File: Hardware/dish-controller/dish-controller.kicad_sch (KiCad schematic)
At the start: 24 parts

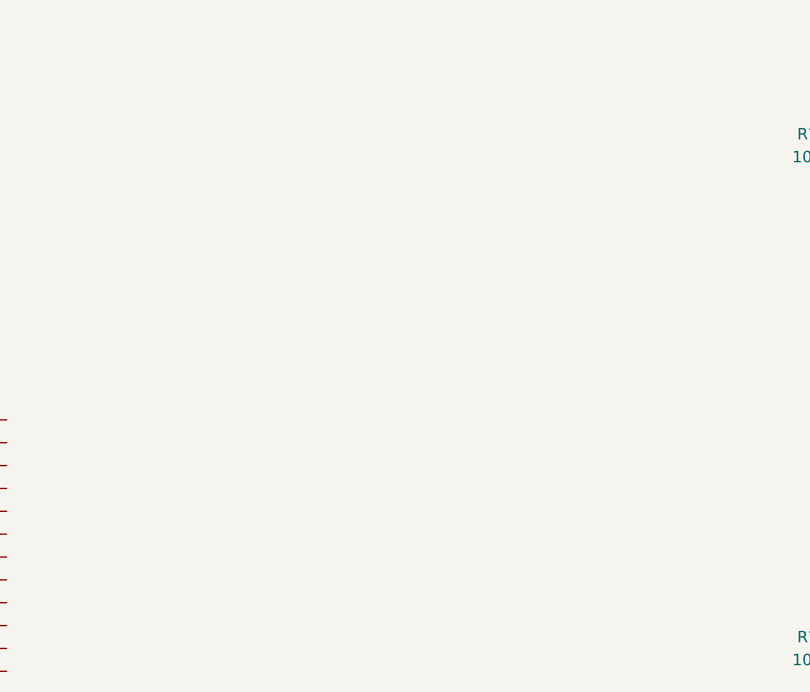
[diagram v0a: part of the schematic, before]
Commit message: Create encoder
COTS encoders are too expensive, so we are creating our own.
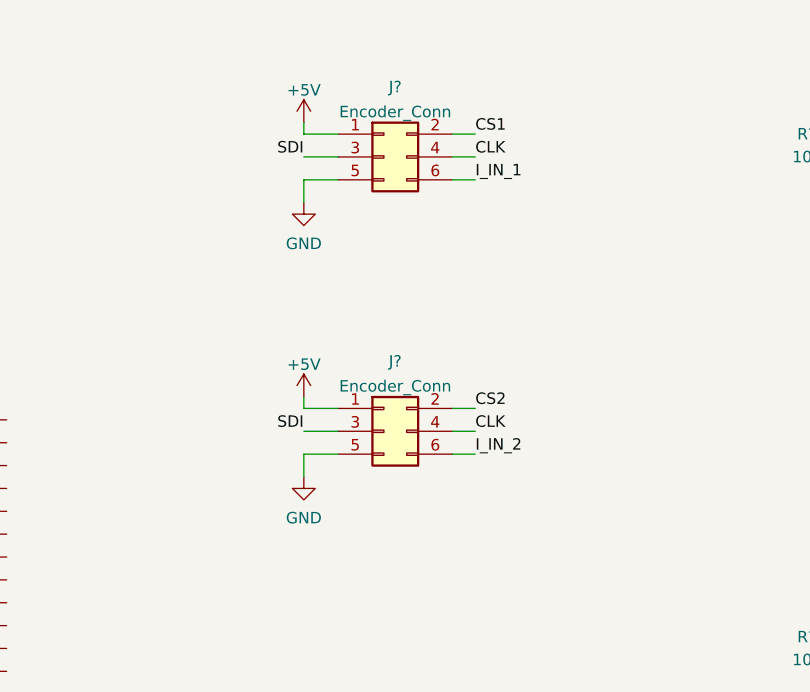
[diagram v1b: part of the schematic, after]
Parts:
- added J? (x2): Encoder_Conn, symbol Connector_Generic:Conn_02x03_Odd_Even
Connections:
- net +5V: now also J?.1 (Pin_1), J?.1 (Pin_1)
- net GND: now also J?.5 (Pin_5), J?.5 (Pin_5)
- new net CLK: J?.4 (Pin_4), J?.4 (Pin_4)
- new net CS1: J?.2 (Pin_2)
- new net CS2: J?.2 (Pin_2)
- new net I_IN_1: J?.6 (Pin_6)
- new net I_IN_2: J?.6 (Pin_6)
- new net SDI: J?.3 (Pin_3), J?.3 (Pin_3)

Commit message: Dish Controller ERC Pass
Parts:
- removed J? (x2): Encoder_Conn, symbol Connector_Generic:Conn_02x03_Odd_Even
- removed J?: Pi_GPIO, symbol Connector_Generic:Conn_02x20_Odd_Even
- removed R? (x8): 10k, symbol Device:R_Small
- added C1, C2, C3: 100u, symbol Device:C_Polarized_US
- added D1, D2, D3, D4: LED_Small, symbol Device:LED_Small
- added G1: DSES-Logo, interferometer:dses-logo, symbol interferometer:DSES-Logo
- added J3, J4: Encoder_Conn, symbol Connector_Generic:Conn_02x04_Odd_Even
- added R1: 3.3k, symbol Device:R_Small
- added R2: 10k, symbol Device:R_Small
- added R3, R4: 2k, symbol Device:R_Small
- added TP1, TP2, TP3, TP4, TP5, TP6, TP7, TP8, TP9: TestPoint, symbol Connector:TestPoint
- added U2: 74HCT541, symbol 74xx:74HCT541
- gave numbers to parts that had none: 15
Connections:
- net +12V: now also C1.1, C3.1, D2.2 (A)
- net +3V3: now also U1.1 (3V3)
- net +5V: now also U1.2 (5V), U1.4 (5V), C2.1, D1.2 (A), J3.1 (Pin_1), J4.1 (Pin_1), U2.20 (VCC)
- net A11: now also U1.33 (GPIO13)
- net A12: now also U1.37 (GPIO26)
- net A21: now also U1.35 (GPIO19)
- net A22: now also U1.40 (GPIO21)
- net CLK: now also U1.23 (GPIO11), TP5.1
- net GND: now also U1.14 (GND), U1.20 (GND), U1.25 (GND), U1.30 (GND), U1.34 (GND), U1.39 (GND), U1.6 (GND), U1.9 (GND), C1.2, C2.2, C3.2, J3.7 (Pin_7), J3.8 (Pin_8), J4.7 (Pin_7), J4.8 (Pin_8), R1.1, R2.2, R3.2, R4.1, U2.10 (GND)
- net IN11: now also U1.13 (GPIO27), TP1.1
- net IN12: now also U1.29 (GPIO5), TP6.1
- net IN21: now also U1.15 (GPIO22), TP2.1
- net IN22: now also U1.31 (GPIO6), TP7.1
- net PWM1: now also U1.3 (GPIO2)
- net PWM2: now also U1.5 (GPIO3)
- net SDI: now also U1.19 (GPIO10), TP3.1
- net STB1: now also U1.7 (GPIO4)
- net STB2: now also U1.11 (GPIO17)
- new net: D2.1 (K), R2.1
- new net: D3.1 (K), R3.1
- new net: D3.2 (A), U1.10 (GPIO15)
- new net: D1.1 (K), R1.2
- new net: D4.1 (K), R4.2
- new net: D4.2 (A), U1.12 (GPIO18)
- new net CLK_OUT: J3.4 (Pin_4), J4.4 (Pin_4), U2.17 (Y1)
- new net EPWM1_IN: J4.6 (Pin_6), U2.8 (A6)
- new net EPWM2_IN: J3.6 (Pin_6), U2.9 (A7)
- new net E_~{EN}: U1.38 (GPIO20), U2.1 (G1), U2.19 (G2)
- new net Logic Level Shift 1/HV1: U2.2 (A0)
- new net Logic Level Shift 1/HV2: U2.3 (A1)
- new net Logic Level Shift 1/HV3: U2.4 (A2)
- new net Logic Level Shift 1/HV4: U2.5 (A3)
- new net Logic Level Shift 2/HV1: U2.14 (Y4)
- new net Logic Level Shift 2/HV2: U2.13 (Y5)
- new net Logic Level Shift 2/HV3: U2.12 (Y6)
- new net Logic Level Shift 2/HV4: U2.11 (Y7)
- new net SDI_OUT: J3.2 (Pin_2), J4.2 (Pin_2), U2.18 (Y0)
- new net SDO: TP4.1, U1.21 (GPIO9)
- new net SDO_IN1: J4.3 (Pin_3), U2.6 (A4)
- new net SDO_IN2: J3.3 (Pin_3), U2.7 (A5)
- new net ~{CS}1: TP8.1, U1.24 (GPIO8)
- new net ~{CS}1_OUT: J4.5 (Pin_5), U2.16 (Y2)
- new net ~{CS}2: TP9.1, U1.26 (GPIO7)
- new net ~{CS}2_OUT: J3.5 (Pin_5), U2.15 (Y3)
- no-connect marks 0 -> 9
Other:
- added sheet Logic Level Shift 1 (level-shift.kicad_sch)
- added sheet Logic Level Shift 2 (level-shift.kicad_sch)
- note added: "Encoder Connectors"
- note added: "Motor Drivers"
- note added: "Power Supply"
- note added: "SPI signals refer to dataflow direction on the encoder IC SDI <-> SDI SDO <-> SDO CLK <-> CLK"
- note added: "Signal Conditioning"
- moved on the sheet: C4, C5, J1, J2, J5, J6, R10, R5, R6, R7, R8, R9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

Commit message: Dish Control: DRC Pass
Floorplanning and routing for dish control PCB complete
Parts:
- added C6: 0.1u, Capacitor_SMD:C_1206_3216Metric, symbol Device:C_Small
- added C7: 1u, Capacitor_SMD:C_0805_2012Metric, symbol Device:C_Small
- C1, C2, C3: footprint (none) -> Capacitor_THT:CP_Radial_D8.0mm_P3.50mm
- C4, C5: footprint (none) -> Capacitor_SMD:C_1206_3216Metric
- D1, D2, D3, D4: footprint (none) -> LED_SMD:LED_0805_2012Metric
- J1, J2, J5, J6: footprint (none) -> TerminalBlock_Phoenix:TerminalBlock_Phoenix_MKDS-3-2-5.08_1x02_P5.08mm_Horizontal
- J3, J4: footprint (none) -> Connector_Molex:Molex_Micro-Fit_3.0_43045-0812_2x04_P3.00mm_Vertical
- R1, R10, R2, R3, R4, R5, R6, R7, R8, R9: footprint (none) -> Resistor_SMD:R_0603_1608Metric
- TP1, TP2, TP3, TP4, TP5, TP6, TP7, TP8, TP9: footprint (none) -> TestPoint:TestPoint_Bridge_Pitch2.54mm_Drill1.0mm
- U1: footprint (none) -> interferometer:raspberry_pi_4
- U2: footprint (none) -> Package_SO:TSSOP-20_4.4x6.5mm_P0.65mm
- U3, U4: footprint (none) -> interferometer:HZIP25-P-1.00F
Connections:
- net Logic Level Shift 1/HV1 is gone; now on net SDI: U2.2 (A0)
- net Logic Level Shift 1/HV2 is gone; now on net CLK: U2.3 (A1)
- net Logic Level Shift 1/HV3 is gone; now on net ~{CS}1: U2.4 (A2)
- net Logic Level Shift 1/HV4 is gone; now on net ~{CS}2: U2.5 (A3)
- net +5V: now also C6.2, C7.2
- net GND: now also C6.1, C7.1
- net EL-2: now reaches J6.1 (Pin_1), U4.10 (OUT2B), U4.14 (OUT2A)
- net EL-1: now reaches J6.2 (Pin_2), U4.12 (OUT1B), U4.16 (OUT1A)
- net AZ-2: now reaches J5.1 (Pin_1), U3.10 (OUT2B), U3.14 (OUT2A)
- net AZ-1: now reaches J5.2 (Pin_2), U3.12 (OUT1B), U3.16 (OUT1A)
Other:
- removed sheet Logic Level Shift 1

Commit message: Dish Controller: Update 3D Model
Added models for the raspberry pi and heatsinks.
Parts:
- added H1: MountingHole, MountingHole:MountingHole_3.2mm_M3, symbol Mechanical:MountingHole
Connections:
- net EPWM1: now also U1.16 (GPIO23)
- net EPWM2: now also U1.18 (GPIO24)
- no-connect marks 9 -> 7
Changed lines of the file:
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@@
     (comment 1 "Designed by Hans Gaensbauer")
   )
-  (junction (at 120.65 147.955) (diameter 0) (color 0 0 0 0)
+  (junction (at 125.095 147.955) (diameter 0) (color 0 0 0 0)
   )
   (junction (at 26.67 57.785) (diameter 0) (color 0 0 0 0)
@@
   (no_connect (at 113.03 158.115))
   (no_connect (at 113.03 132.715))
-  (no_connect (at 113.03 145.415))
-  (no_connect (at 113.03 142.875))
   (no_connect (at 113.03 168.275))
   (no_connect (at 113.03 163.195))
@@
     (stroke (width 0) (type default) (color 0 0 0 0))
   )
+  (wire (pts (xy 113.03 145.415) (xy 115.57 145.415))
+    (stroke (width 0) (type default) (color 0 0 0 0))
+  )
   (wire (pts (xy 153.035 67.31) (xy 153.035 68.58))
     (stroke (width 0) (type default) (color 0 0 0 0))
@@
     (stroke (width 0) (type default) (color 0 0 0 0))
   )
-  (wire (pts (xy 120.65 140.335) (xy 120.65 147.955))
+  (wire (pts (xy 125.095 140.335) (xy 125.095 147.955))
     (stroke (width 0) (type default) (color 0 0 0 0))
   )
@@
     (stroke (width 0) (type default) (color 0 0 0 0))
   )
+  (wire (pts (xy 113.03 142.875) (xy 115.57 142.875))
+    (stroke (width 0) (type default) (color 0 0 0 0))
+  )
   (wire (pts (xy 245.745 93.345) (xy 250.825 93.345))
     (stroke (width 0) (type default) (color 0 0 0 0))
@@
     (stroke (width 0) (type default) (color 0 0 0 0))
   )
-  (wire (pts (xy 113.03 147.955) (xy 120.65 147.955))
+  (wire (pts (xy 113.03 147.955) (xy 125.095 147.955))
     (stroke (width 0) (type default) (color 0 0 0 0))
   )
@@
     (stroke (width 0) (type default) (color 0 0 0 0))
   )
-  (wire (pts (xy 120.65 149.225) (xy 120.65 147.955))
+  (wire (pts (xy 125.095 149.225) (xy 125.095 147.955))
     (stroke (width 0) (type default) (color 0 0 0 0))
   )
@@
     (stroke (width 0) (type default) (color 0 0 0 0))
   )
-  (wire (pts (xy 113.03 140.335) (xy 120.65 140.335))
+  (wire (pts (xy 113.03 140.335) (xy 125.095 140.335))
     (stroke (width 0) (type default) (color 0 0 0 0))
   )
@@
     (effects (font (size 1.27 1.27)) (justify right bottom))
   )
+  (label "EPWM1" (at 115.57 142.875 0)
+    (effects (font (size 1.27 1.27)) (justify left bottom))
+  )
   (label "A22" (at 197.485 108.585 270)
     (effects (font (size 1.27 1.27)) (justify right bottom))
@@
   (label "SDI" (at 104.775 57.15 180)
     (effects (font (size 1.27 1.27)) (justify right bottom))
+  )
+  (label "EPWM2" (at 115.57 145.415 0)
+    (effects (font (size 1.27 1.27)) (justify left bottom))
   )
   (label "IN22" (at 83.82 163.195 180)
@@
     (pin "1")
   )
-  (symbol (lib_id "power:GND") (at 120.65 149.225 0) (mirror y) (unit 1)
-    (in_bom yes) (on_board yes) (fields_autoplaced)
-    (property "Reference" "#PWR0116" (id 0) (at 120.65 155.575 0)
-      (effects (font (size 1.27 1.27)) hide)
-    )
-    (property "Value" "GND" (id 1) (at 120.171 148.59 90)
+  (symbol (lib_id "power:GND") (at 125.095 149.225 0) (mirror y) (unit 1)
+    (in_bom yes) (on_board yes) (fields_autoplaced)
+    (property "Reference" "#PWR0116" (id 0) (at 125.095 155.575 0)
+      (effects (font (size 1.27 1.27)) hide)
+    )
+    (property "Value" "GND" (id 1) (at 124.616 148.59 90)
       (effects (font (size 1.27 1.27)) (justify left) hide)
     )
-    (property "Footprint" "" (id 2) (at 120.65 149.225 0)
-      (effects (font (size 1.27 1.27)) hide)
-    )
-    (property "Datasheet" "" (id 3) (at 120.65 149.225 0)
+    (property "Footprint" "" (id 2) (at 125.095 149.225 0)
+      (effects (font (size 1.27 1.27)) hide)
+    )
+    (property "Datasheet" "" (id 3) (at 125.095 149.225 0)
       (effects (font (size 1.27 1.27)) hide)
     )
@@
     )
     (pin "1")
+  )
+  (symbol (lib_id "Mechanical:MountingHole") (at 40.64 130.175 0) (unit 1)
+    (in_bom yes) (on_board yes) (fields_autoplaced)
+    (property "Reference" "H1" (id 0) (at 43.18 129.2665 0)
+      (effects (font (size 1.27 1.27)) (justify left))
+    )
+    (property "Value" "MountingHole" (id 1) (at 43.18 132.0416 0)
+      (effects (font (size 1.27 1.27)) (justify left))
+    )
+    (property "Footprint" "MountingHole:MountingHole_3.2mm_M3" (id 2) (at 40.64 130.175 0)
+      (effects (font (size 1.27 1.27)) hide)
+    )
+    (property "Datasheet" "~" (id 3) (at 40.64 130.175 0)
+      (effects (font (size 1.27 1.27)) hide)
+    )
   )
   (symbol (lib_id "power:GND") (at 231.775 61.595 0) (unit 1)
@@
       (reference "G1") (unit 1) (value "DSES-Logo") (footprint "interferometer:dses-logo")
     )
+    (path "/6afa16aa-3a0d-488e-9562-28586553ebba"
+      (reference "H1") (unit 1) (value "MountingHole") (footprint "MountingHole:MountingHole_3.2mm_M3")
+    )
     (path "/1b224dc1-21ea-4438-b060-d75fb8e0096a"

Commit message: Dish Controller: Added I2C header
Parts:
- added J7: Conn_01x05_Male, Connector_PinHeader_2.54mm:PinHeader_1x05_P2.54mm_Vertical, symbol Connector:Conn_01x05_Male
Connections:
- net +3V3: now also J7.2 (Pin_2)
- net +5V: now also J7.1 (Pin_1)
- net GND: now also J7.5 (Pin_5)
- net PWM1: now also U1.36 (GPIO16); no longer U1.3 (GPIO2)
- net PWM2: now also U1.32 (GPIO12); no longer U1.5 (GPIO3)
- new net GPIO_2: J7.3 (Pin_3), U1.3 (GPIO2)
- new net GPIO_3: J7.4 (Pin_4), U1.5 (GPIO3)
- no-connect marks 7 -> 5
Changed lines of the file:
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@@
   (no_connect (at 113.03 158.115))
   (no_connect (at 113.03 132.715))
-  (no_connect (at 113.03 168.275))
-  (no_connect (at 113.03 163.195))
   (no_connect (at 86.36 158.115))
   (no_connect (at 86.36 145.415))
@@
     (stroke (width 0) (type default) (color 0 0 0 0))
   )
+  (wire (pts (xy 163.83 149.225) (xy 166.37 149.225))
+    (stroke (width 0) (type default) (color 0 0 0 0))
+  )
   (wire (pts (xy 76.2 160.655) (xy 86.36 160.655))
     (stroke (width 0) (type default) (color 0 0 0 0))
   )
+  (wire (pts (xy 158.115 146.685) (xy 166.37 146.685))
+    (stroke (width 0) (type default) (color 0 0 0 0))
+  )
   (wire (pts (xy 113.03 170.815) (xy 115.57 170.815))
     (stroke (width 0) (type default) (color 0 0 0 0))
@@
     (stroke (width 0) (type default) (color 0 0 0 0))
   )
+  (wire (pts (xy 158.115 142.875) (xy 158.115 146.685))
+    (stroke (width 0) (type default) (color 0 0 0 0))
+  )
   (wire (pts (xy 30.48 52.705) (xy 34.925 52.705))
     (stroke (width 0) (type default) (color 0 0 0 0))
@@
     (stroke (width 0) (type default) (color 0 0 0 0))
   )
+  (wire (pts (xy 113.03 168.275) (xy 115.57 168.275))
+    (stroke (width 0) (type default) (color 0 0 0 0))
+  )
   (wire (pts (xy 248.285 53.975) (xy 248.285 51.435))
     (stroke (width 0) (type default) (color 0 0 0 0))
@@
     (stroke (width 0) (type default) (color 0 0 0 0))
   )
+  (wire (pts (xy 113.03 163.195) (xy 115.57 163.195))
+    (stroke (width 0) (type default) (color 0 0 0 0))
+  )
   (wire (pts (xy 112.395 29.845) (xy 114.935 29.845))
     (stroke (width 0) (type default) (color 0 0 0 0))
@@
     (stroke (width 0) (type default) (color 0 0 0 0))
   )
+  (wire (pts (xy 163.83 158.115) (xy 163.83 154.305))
+    (stroke (width 0) (type default) (color 0 0 0 0))
+  )
   (wire (pts (xy 197.485 45.085) (xy 197.485 46.355))
     (stroke (width 0) (type default) (color 0 0 0 0))
@@
     (stroke (width 0) (type default) (color 0 0 0 0))
   )
+  (wire (pts (xy 163.195 140.97) (xy 163.195 144.145))
+    (stroke (width 0) (type default) (color 0 0 0 0))
+  )
   (wire (pts (xy 87.63 30.48) (xy 90.17 30.48))
     (stroke (width 0) (type default) (color 0 0 0 0))
@@
     (stroke (width 0) (type default) (color 0 0 0 0))
   )
+  (wire (pts (xy 163.83 151.765) (xy 166.37 151.765))
+    (stroke (width 0) (type default) (color 0 0 0 0))
+  )
+  (wire (pts (xy 163.195 144.145) (xy 166.37 144.145))
+    (stroke (width 0) (type default) (color 0 0 0 0))
+  )
   (wire (pts (xy 29.21 32.385) (xy 29.21 33.655))
     (stroke (width 0) (type default) (color 0 0 0 0))
@@
   )
   (wire (pts (xy 113.03 155.575) (xy 123.19 155.575))
+    (stroke (width 0) (type default) (color 0 0 0 0))
+  )
+  (wire (pts (xy 163.83 154.305) (xy 166.37 154.305))
     (stroke (width 0) (type default) (color 0 0 0 0))
   )
@@
     (effects (font (size 1.27 1.27)) (justify right bottom))
   )
-  (label "PWM1" (at 83.82 127.635 180)
-    (effects (font (size 1.27 1.27)) (justify right bottom))
+  (label "PWM1" (at 115.57 168.275 0)
+    (effects (font (size 1.27 1.27)) (justify left bottom))
   )
   (label "STB2" (at 83.82 137.795 180)
@@
     (effects (font (size 1.27 1.27)) (justify left bottom))
   )
-  (label "PWM2" (at 83.82 130.175 180)
-    (effects (font (size 1.27 1.27)) (justify right bottom))
+  (label "PWM2" (at 115.57 163.195 0)
+    (effects (font (size 1.27 1.27)) (justify left bottom))
   )
   (label "SDI_OUT" (at 130.175 27.305 0)
@@
     (effects (font (size 1.27 1.27)) (justify right bottom))
   )
+  (label "GPIO_2" (at 163.83 149.225 180)
+    (effects (font (size 1.27 1.27)) (justify right bottom))
+  )
   (label "PWM1" (at 216.535 56.515 270)
     (effects (font (size 1.27 1.27)) (justify right bottom))
   )
+  (label "GPIO_2" (at 83.82 127.635 180)
+    (effects (font (size 1.27 1.27)) (justify right bottom))
+  )
   (label "E_~{EN}" (at 115.57 170.815 0)
     (effects (font (size 1.27 1.27)) (justify left bottom))
@@
     (effects (font (size 1.27 1.27)) (justify right bottom))
   )
+  (label "GPIO_3" (at 163.83 151.765 180)
+    (effects (font (size 1.27 1.27)) (justify right bottom))
+  )
   (label "EPWM1" (at 115.57 142.875 0)
     (effects (font (size 1.27 1.27)) (justify left bottom))
@@
   )
   (label "CLK" (at 83.82 153.035 180)
+    (effects (font (size 1.27 1.27)) (justify right bottom))
+  )
+  (label "GPIO_3" (at 83.82 130.175 180)
     (effects (font (size 1.27 1.27)) (justify right bottom))
   )
@@
     (pin "8")
   )
+  (symbol (lib_id "power:+3.3V") (at 158.115 142.875 0) (unit 1)
+    (in_bom yes) (on_board yes) (fields_autoplaced)
+    (property "Reference" "#PWR01" (id 0) (at 158.115 146.685 0)
+      (effects (font (size 1.27 1.27)) hide)
+    )
+    (property "Value" "+3.3V" (id 1) (at 158.115 139.2705 0))
+    (property "Footprint" "" (id 2) (at 158.115 142.875 0)
+      (effects (font (size 1.27 1.27)) hide)
+    )
+    (property "Datasheet" "" (id 3) (at 158.115 142.875 0)
+      (effects (font (size 1.27 1.27)) hide)
+    )
+    (pin "1")
+  )
   (symbol (lib_id "power:+3.3V") (at 197.485 100.965 0) (unit 1)
     (in_bom yes) (on_board yes) (fields_autoplaced)
@@
     (pin "1")
   )
+  (symbol (lib_id "power:+5V") (at 163.195 140.97 0) (unit 1)
+    (in_bom yes) (on_board yes) (fields_autoplaced)
+    (property "Reference" "#PWR02" (id 0) (at 163.195 144.78 0)
+      (effects (font (size 1.27 1.27)) hide)
+    )
+    (property "Value" "+5V" (id 1) (at 163.195 137.3655 0))
+    (property "Footprint" "" (id 2) (at 163.195 140.97 0)
+      (effects (font (size 1.27 1.27)) hide)
+    )
+    (property "Datasheet" "" (id 3) (at 163.195 140.97 0)
+      (effects (font (size 1.27 1.27)) hide)
+    )
+    (pin "1")
+  )
   (symbol (lib_id "Connector:TestPoint") (at 76.2 150.495 90) (unit 1)
     (in_bom yes) (on_board yes)
@@
     )
     (property "Datasheet" "" (id 3) (at 29.21 33.655 0)
+      (effects (font (size 1.27 1.27)) hide)
+    )
+    (pin "1")
+  )
+  (symbol (lib_id "power:GND") (at 163.83 158.115 0) (unit 1)
+    (in_bom yes) (on_board yes) (fields_autoplaced)
+    (property "Reference" "#PWR03" (id 0) (at 163.83 164.465 0)
+      (effects (font (size 1.27 1.27)) hide)
+    )
+    (property "Value" "GND" (id 1) (at 164.309 157.48 90)
+      (effects (font (size 1.27 1.27)) (justify left) hide)
+    )
+    (property "Footprint" "" (id 2) (at 163.83 158.115 0)
+      (effects (font (size 1.27 1.27)) hide)
+    )
+    (property "Datasheet" "" (id 3) (at 163.83 158.115 0)
       (effects (font (size 1.27 1.27)) hide)
     )
@@
     (pin "1")
   )
+  (symbol (lib_id "Connector:Conn_01x05_Male") (at 171.45 149.225 0) (mirror y) (unit 1)
+    (in_bom yes) (on_board yes) (fields_autoplaced)
+    (property "Reference" "J7" (id 0) (at 172.1612 148.3165 0)
+      (effects (font (size 1.27 1.27)) (justify right))
+    )
+    (property "Value" "Conn_01x05_Male" (id 1) (at 172.1612 151.0916 0)
+      (effects (font (size 1.27 1.27)) (justify right))
+    )
+    (property "Footprint" "Connector_PinHeader_2.54mm:PinHeader_1x05_P2.54mm_Vertical" (id 2) (at 171.45 149.225 0)
+      (effects (font (size 1.27 1.27)) hide)
+    )
+    (property "Datasheet" "~" (id 3) (at 171.45 149.225 0)
+      (effects (font (size 1.27 1.27)) hide)
+    )
+    (pin "1")
+    (pin "2")
+    (pin "3")
+    (pin "4")
+    (pin "5")
+  )
   (sheet (at 136.525 66.04) (size 12.7 10.16)
     (stroke (width 0.1524) (type solid) (color 0 0 0 0))
@@
       (reference "#FLG0103") (unit 1) (value "PWR_FLAG") (footprint "")
     )
+    (path "/21430cf8-54eb-4698-af2e-0dec19277f45"
+      (reference "#PWR01") (unit 1) (value "+3.3V") (footprint "")
+    )
+    (path "/72872ae8-9abc-4293-a1b2-1e5e325b929e"
+      (reference "#PWR02") (unit 1) (value "+5V") (footprint "")
+    )
+    (path "/8ed50312-f0ab-490d-b296-a6e26bd31d60"
+      (reference "#PWR03") (unit 1) (value "GND") (footprint "")
+    )
     (path "/6acc2c78-0f6c-4dee-bea2-8f761e9ecbc9"
       (reference "#PWR0101") (unit 1) (value "+5V") (footprint "")
@@
       (reference "J6") (unit 1) (value "EL-OUT") (footprint "TerminalBlock_Phoenix:TerminalBlock_Phoenix_MKDS-3-2-5.08_1x02_P5.08mm_Horizontal")
     )
+    (path "/fc0a8c99-b5f0-411a-862f-c11f70d3d167"
+      (reference "J7") (unit 1) (value "Conn_01x05_Male") (footprint "Connector_PinHeader_2.54mm:PinHeader_1x05_P2.54mm_Vertical")
+    )
     (path "/6b63c3f1-cb79-43f4-b3b7-e06a4c338b30/e39a47ca-19da-4b40-b8f6-a156ead87dab"
